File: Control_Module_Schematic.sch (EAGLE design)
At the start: 30 parts, among them U2 ATMEGA328P_TQFP

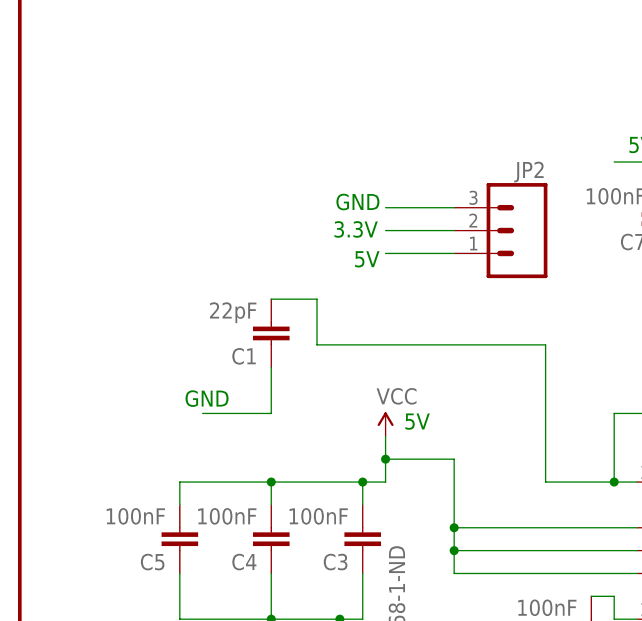
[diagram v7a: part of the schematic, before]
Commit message: Added tactile switch for reset
Also did some manual routing optimizations
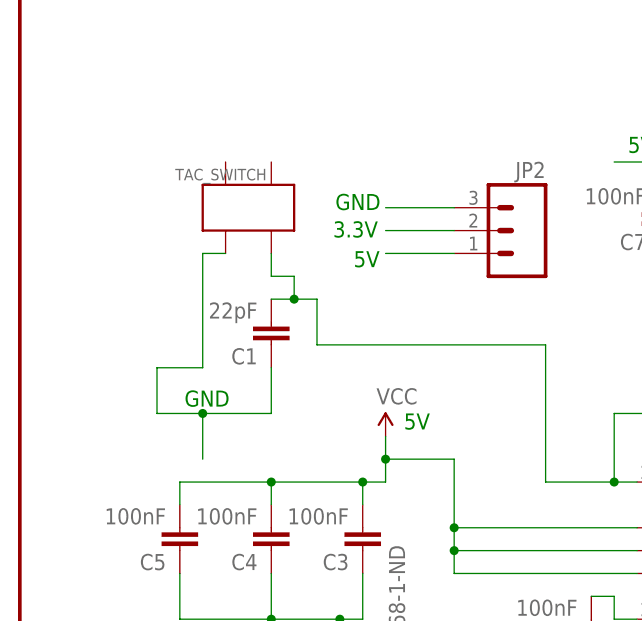
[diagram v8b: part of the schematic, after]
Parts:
- added TAC_SWITCH: TACTILE_SWITCH, WHCS:TACTILE_SWITCH
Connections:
- net GND: now also TAC_SWITCH.P$2
- net N$24: now also TAC_SWITCH.P$4
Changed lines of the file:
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@@
 <part name="JP4" library="SparkFun-Connectors" deviceset="M10" device="LOCK_LONGPADS"/>
 <part name="FRAME1" library="WHCS" deviceset="FRAME-LETTER" device="NO_PACKAGE"/>
+<part name="TAC_SWITCH" library="WHCS" deviceset="TACTILE_SWITCH" device=""/>
 </parts>
 <sheets>
@@
 <instance part="FRAME1" gate="G$1" x="-121.92" y="-71.12"/>
 <instance part="FRAME1" gate="V" x="5.08" y="-68.58"/>
+<instance part="TAC_SWITCH" gate="G$1" x="-96.52" y="55.88"/>
 </instances>
 <busses>
@@
 </segment>
 <segment>
-<pinref part="C1" gate="G$1" pin="1"/>
-<wire x1="-93.98" y1="38.1" x2="-93.98" y2="33.02" width="0.1524" layer="91"/>
-<wire x1="-93.98" y1="33.02" x2="-101.6" y2="33.02" width="0.1524" layer="91"/>
-</segment>
-<segment>
 <pinref part="U$1" gate="G$1" pin="GND"/>
 <wire x1="-40.64" y1="53.34" x2="-40.64" y2="45.72" width="0.1524" layer="91"/>
@@
 <wire x1="73.66" y1="17.78" x2="73.66" y2="15.24" width="0.1524" layer="91"/>
 </segment>
+<segment>
+<wire x1="-93.98" y1="33.02" x2="-101.6" y2="33.02" width="0.1524" layer="91"/>
+<pinref part="C1" gate="G$1" pin="1"/>
+<wire x1="-93.98" y1="38.1" x2="-93.98" y2="33.02" width="0.1524" layer="91"/>
+<wire x1="-101.6" y1="27.94" x2="-101.6" y2="33.02" width="0.1524" layer="91"/>
+<wire x1="-101.6" y1="33.02" x2="-106.68" y2="33.02" width="0.1524" layer="91"/>
+<junction x="-101.6" y="33.02"/>
+<wire x1="-106.68" y1="33.02" x2="-106.68" y2="38.1" width="0.1524" layer="91"/>
+<wire x1="-106.68" y1="38.1" x2="-101.6" y2="38.1" width="0.1524" layer="91"/>
+<wire x1="-101.6" y1="38.1" x2="-101.6" y2="50.8" width="0.1524" layer="91"/>
+<pinref part="TAC_SWITCH" gate="G$1" pin="P$2"/>
+<wire x1="-101.6" y1="50.8" x2="-99.06" y2="50.8" width="0.1524" layer="91"/>
+</segment>
 </net>
 <net name="N$5" class="0">
@@
 <segment>
 <pinref part="C1" gate="G$1" pin="2"/>
-<wire x1="-88.9" y1="45.72" x2="-93.98" y2="45.72" width="0.1524" layer="91"/>
 <wire x1="-88.9" y1="40.64" x2="-88.9" y2="45.72" width="0.1524" layer="91"/>
 <pinref part="U2" gate="U$1" pin="PC6(/RESET)"/>
@@
 <wire x1="63.5" y1="-5.08" x2="63.5" y2="53.34" width="0.1524" layer="91"/>
 <wire x1="45.72" y1="53.34" x2="63.5" y2="53.34" width="0.1524" layer="91"/>
-</segment>
-</net>
+<wire x1="-88.9" y1="45.72" x2="-91.44" y2="45.72" width="0.1524" layer="91"/>
+<pinref part="TAC_SWITCH" gate="G$1" pin="P$4"/>
+<wire x1="-91.44" y1="45.72" x2="-93.98" y2="45.72" width="0.1524" layer="91"/>
+<wire x1="-93.98" y1="50.8" x2="-93.98" y2="48.26" width="0.1524" layer="91"/>
+<wire x1="-93.98" y1="48.26" x2="-91.44" y2="48.26" width="0.1524" layer="91"/>
+<wire x1="-91.44" y1="48.26" x2="-91.44" y2="45.72" width="0.1524" layer="91"/>
+<junction x="-91.44" y="45.72"/>
+</segment>
+</net>
